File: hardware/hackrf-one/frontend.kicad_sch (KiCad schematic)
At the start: 141 parts, among them J2 RF-SHIELD-FRAME, J3 RF-SHIELD-COVER, J4 MOUNTING_HOLE, J5 MOUNTING_HOLE, J6 MOUNTING_HOLE, J7 MOUNTING_HOLE, J8 MOUNTING_HOLE, J9 MOUNTING_HOLE, P13 GPO1, P19 GPO3, P27 MIXER_SDATA, P31 MIXER_SCLK, P32 MIXER_ENX, P33 MIXER_RESETX, P34 MIX_BYPASS, P35 !MIX_BYPASS, P4 ANTENNA, P43 RX, P44 HP, P45 LP, P46 TX_MIX_BP, P47 RX_MIX_BP, P48 TX_AMP, P49 RX_AMP, P50 AMP_BYPASS, P51 !TX_AMP_PWR, P52 !RX_AMP_PWR, P6 GPO4, Q1 MOSFET_P, Q2 MOSFET_P, Q4 MOSFET_P, T1 MIX_IN_BALUN, T2 MIX_OUT_BALUN, U1 SKY13453, U10 SKY13453, U11 SKY13453, U12 SKY13317, U13 MGA-81563, U14 SKY13317, U2 SKY13453, U25 MGA-81563, U3 RX_LOWPASS_FILTER, U4 RFFC5072, U5 SKY13453, U6 SKY13453, U7 SKY13453, U8 RX_HIGHPASS_FILTER, U9 SKY13317

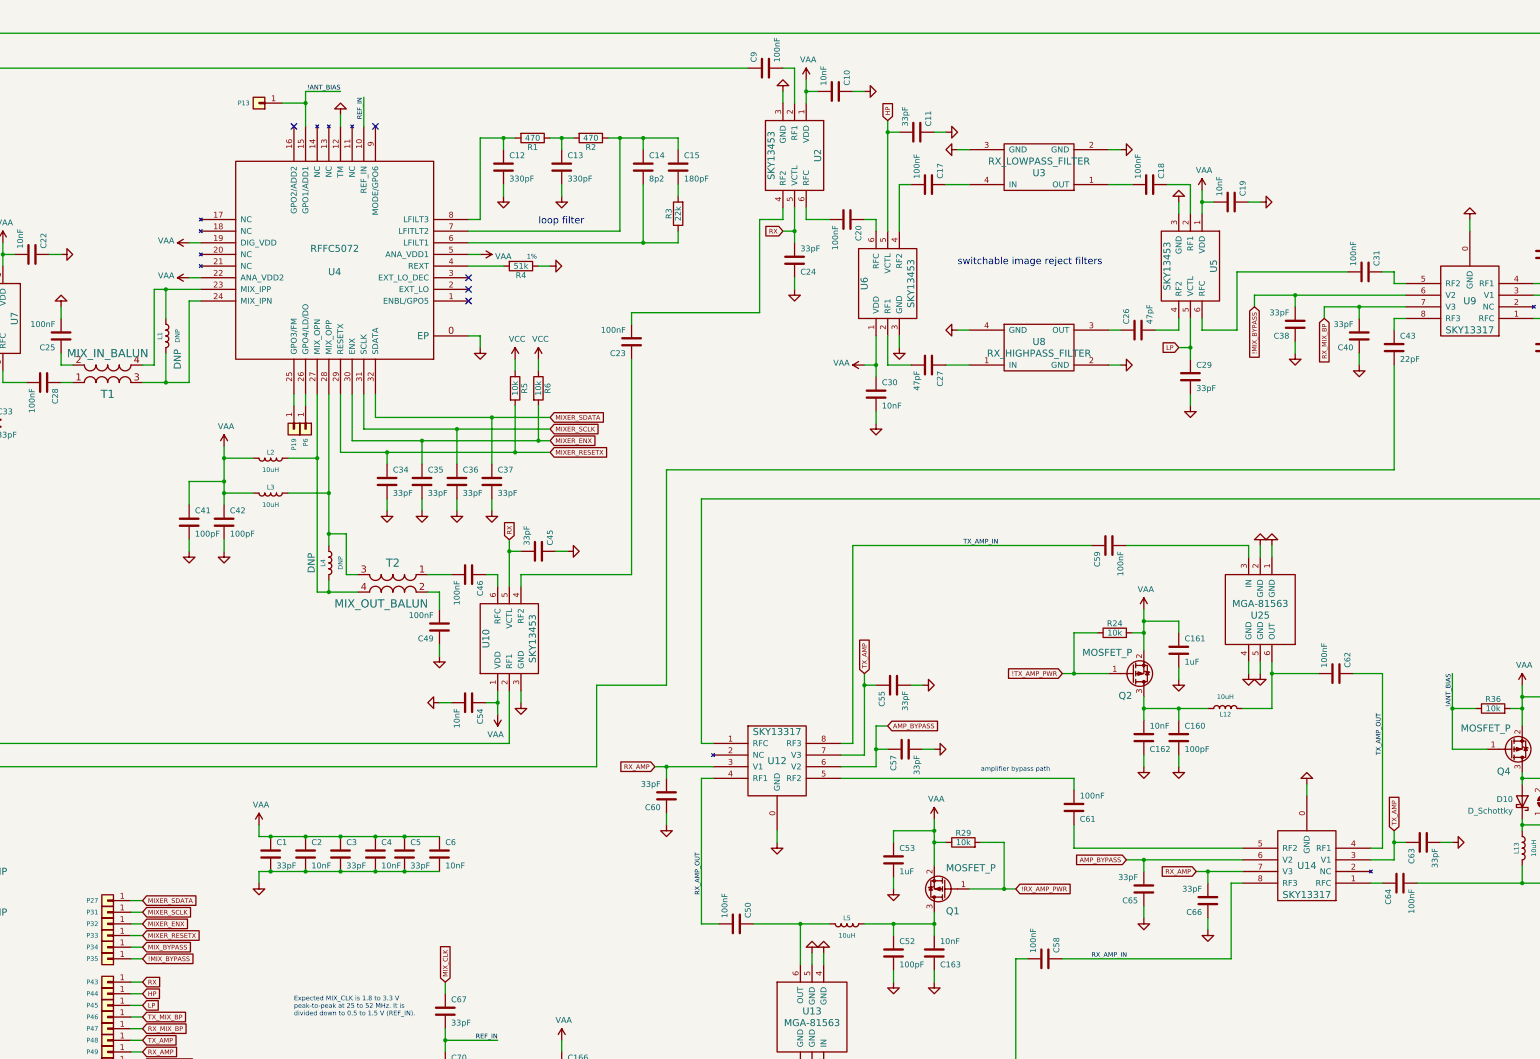
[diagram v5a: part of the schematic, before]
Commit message: HackRF One: move !ANT_BIAS control from U4 to U23
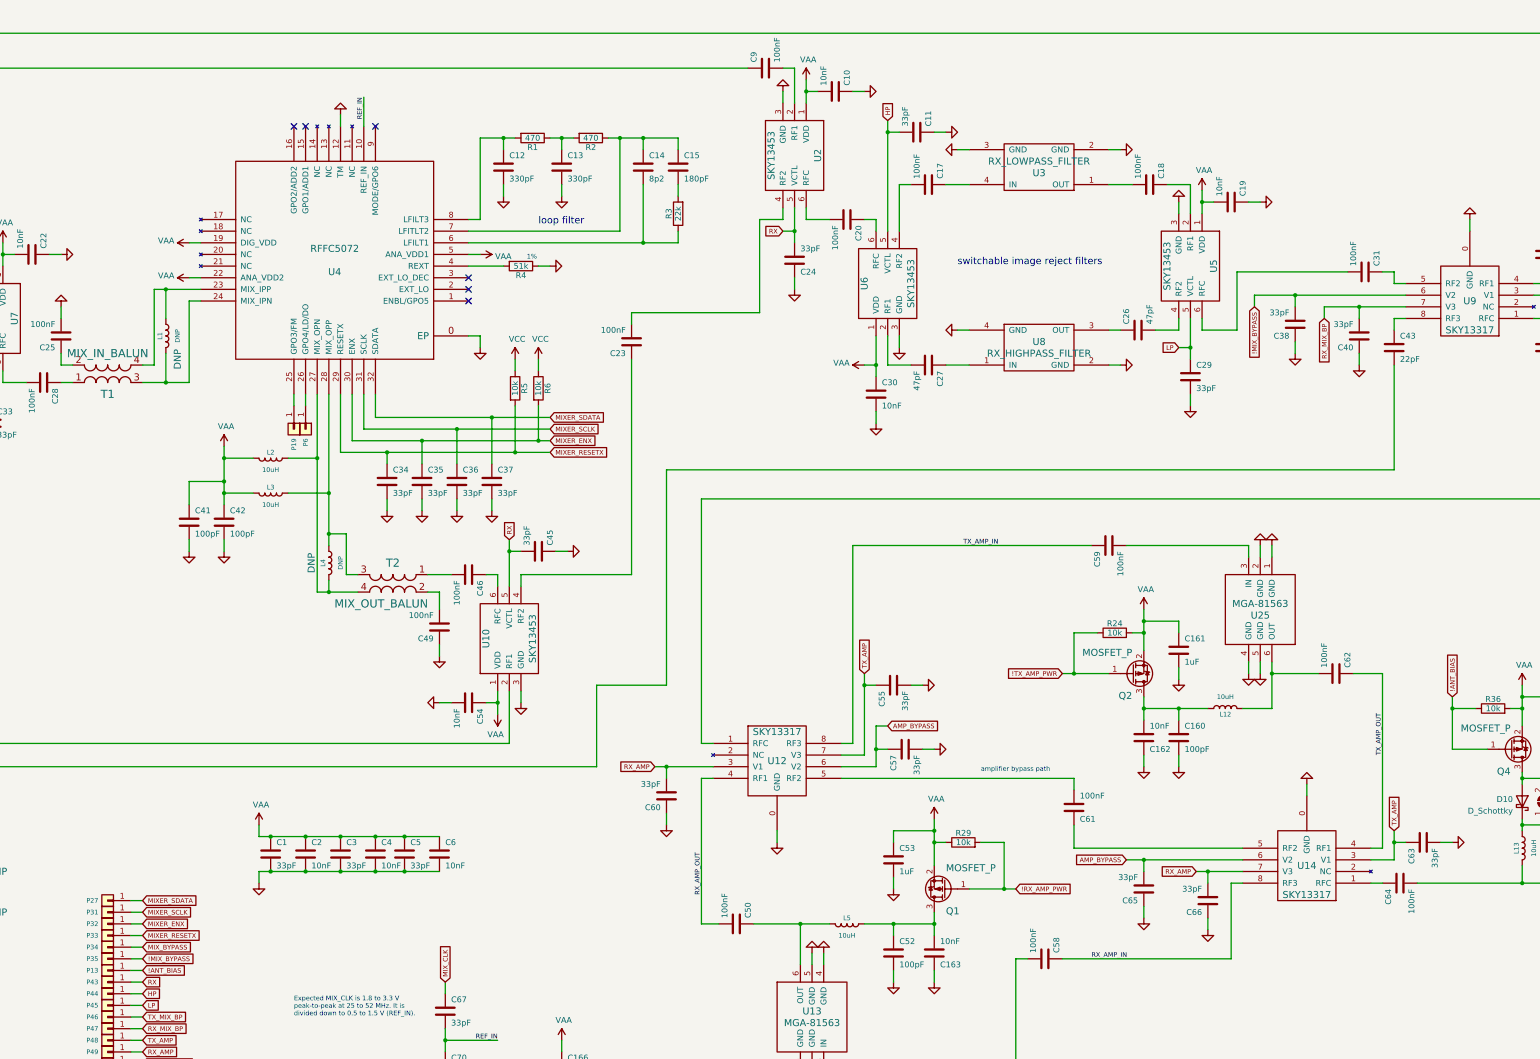
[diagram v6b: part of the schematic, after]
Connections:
- net !ANT_BIAS: no longer U4.15 (GPO1/ADD1)
- no-connect marks 5 -> 6
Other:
- moved on the sheet: P13
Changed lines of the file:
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@@
   (junction (at 160.02 248.92) (diameter 0) (color 0 0 0 0)
   )
-  (junction (at 129.54 44.45) (diameter 0) (color 0 0 0 0)
-  )
   (junction (at 111.76 129.54) (diameter 0) (color 0 0 0 0)
   )
@@
   (no_connect (at 165.1 85.09))
   (no_connect (at 165.1 87.63))
+  (no_connect (at 129.54 49.53))
   (no_connect (at 127 49.53))
   (no_connect (at 144.78 49.53))
@@
     (stroke (width 0) (type default) (color 0 0 0 0))
   )
-  (wire (pts (xy 124.46 44.45) (xy 129.54 44.45))
-    (stroke (width 0) (type default) (color 0 0 0 0))
-  )
   (wire (pts (xy 237.49 223.52) (xy 243.84 223.52))
     (stroke (width 0) (type default) (color 0 0 0 0))
@@
     (stroke (width 0) (type default) (color 0 0 0 0))
   )
-  (wire (pts (xy 129.54 44.45) (xy 129.54 49.53))
-    (stroke (width 0) (type default) (color 0 0 0 0))
-  )
   (wire (pts (xy 147.32 120.65) (xy 175.26 120.65))
     (stroke (width 0) (type default) (color 0 0 0 0))
@@
     (stroke (width 0) (type default) (color 0 0 0 0))
   )
+  (wire (pts (xy 91.44 233.68) (xy 93.98 233.68))
+    (stroke (width 0) (type default) (color 0 0 0 0))
+  )
   (wire (pts (xy 31.75 254) (xy 31.75 256.54))
     (stroke (width 0) (type default) (color 0 0 0 0))
@@
     (stroke (width 0) (type default) (color 0 0 0 0))
   )
-  (wire (pts (xy 129.54 41.91) (xy 137.16 41.91))
-    (stroke (width 0) (type default) (color 0 0 0 0))
-  )
   (wire (pts (xy 134.62 148.59) (xy 134.62 151.13))
     (stroke (width 0) (type default) (color 0 0 0 0))
@@
     (stroke (width 0) (type default) (color 0 0 0 0))
   )
-  (wire (pts (xy 379.73 168.91) (xy 379.73 176.53))
+  (wire (pts (xy 379.73 173.99) (xy 379.73 176.53))
     (stroke (width 0) (type default) (color 0 0 0 0))
   )
@@
     (stroke (width 0) (type default) (color 0 0 0 0))
   )
-  (wire (pts (xy 129.54 41.91) (xy 129.54 44.45))
-    (stroke (width 0) (type default) (color 0 0 0 0))
-  )
   (wire (pts (xy 271.78 93.98) (xy 274.32 93.98))
     (stroke (width 0) (type default) (color 0 0 0 0))
@@
     (effects (font (size 1.016 1.016)) (justify right bottom))
   )
-  (label "!ANT_BIAS" (at 379.73 168.91 270)
-    (effects (font (size 1.016 1.016)) (justify right bottom))
-  )
   (label "TX_AMP_IN" (at 280.67 140.97 180)
     (effects (font (size 1.016 1.016)) (justify right bottom))
   )
-  (label "!ANT_BIAS" (at 137.16 41.91 180)
-    (effects (font (size 1.016 1.016)) (justify right bottom))
-  )
   (label "REF_IN" (at 142.24 43.18 270)
     (effects (font (size 1.016 1.016)) (justify right bottom))
@@
     )
   )
+  (global_label "!ANT_BIAS" (shape input) (at 93.98 233.68 0) (fields_autoplaced)
+    (effects (font (size 1.016 1.016)) (justify left))
+    (property "Intersheet References" "${INTERSHEET_REFS}" (id 0) (at 103.1448 233.6165 0)
+      (effects (font (size 1.016 1.016)) (justify left) hide)
+    )
+  )
   (global_label "TX_IF" (shape input) (at 27.94 29.21 180) (fields_autoplaced)
     (effects (font (size 1.524 1.524)) (justify right))
@@
     )
   )
+  (global_label "!ANT_BIAS" (shape input) (at 379.73 173.99 90) (fields_autoplaced)
+    (effects (font (size 1.016 1.016)) (justify left))
+    (property "Intersheet References" "${INTERSHEET_REFS}" (id 0) (at 379.6665 164.8252 90)
+      (effects (font (size 1.016 1.016)) (justify left) hide)
+    )
+  )
   (global_label "!MIX_BYPASS" (shape input) (at 43.18 22.86 90) (fields_autoplaced)
     (effects (font (size 1.016 1.016)) (justify left))
@@
     (pin "1")
   )
-  (symbol (lib_id "Connector_Generic:Conn_01x01") (at 119.38 44.45 180) (unit 1)
+  (symbol (lib_id "Connector_Generic:Conn_01x01") (at 86.36 233.68 180) (unit 1)
     (in_bom yes) (on_board yes)
-    (property "Reference" "P13" (id 0) (at 117.348 44.45 0)
+    (property "Reference" "P13" (id 0) (at 84.328 233.68 0)
       (effects (font (size 1.016 1.016)) (justify left))
     )
-    (property "Value" "GPO1" (id 1) (at 119.38 45.847 0)
+    (property "Value" "GPO1" (id 1) (at 86.36 235.077 0)
       (effects (font (size 0.762 0.762)) hide)
     )
-    (property "Footprint" "hackrf:GSG-TESTPOINT-50MIL" (id 2) (at 119.38 44.45 0)
+    (property "Footprint" "hackrf:GSG-TESTPOINT-50MIL" (id 2) (at 86.36 233.68 0)
       (effects (font (size 1.524 1.524)) hide)
     )
-    (property "Datasheet" "" (id 3) (at 119.38 44.45 0)
+    (property "Datasheet" "" (id 3) (at 86.36 233.68 0)
       (effects (font (size 1.524 1.524)) hide)
     )
-    (property "Note" "DNP" (id 4) (at 119.38 44.45 0)
+    (property "Note" "DNP" (id 4) (at 86.36 233.68 0)
       (effects (font (size 1.524 1.524)) hide)
     )

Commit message: HackRF One: component selections, DNP, and Notes
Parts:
- C1, C11, C24, C29, C3, C33, C34, C35, C36, C37, C38, C39, C40, C45, C47, C5, C55, C57, C60, C63, C65, C66, C67, C7: Manufacturer Murata -> Samsung; Part Number GRM1555C1H330JA01D -> CL05C330JB5NNNC
- C10, C16, C162, C163, C19, C2, C22, C30, C4, C54, C56, C6: Manufacturer Murata -> Samsung; Part Number GRM155R71C103KA01D -> CL05B103KB5NNNC
- C12, C13: Manufacturer Murata -> Samsung; Part Number GRM155R71H331KA01D -> CL05C331JB5NNNC
- C14: Manufacturer Taiyo Yuden -> Yageo; Part Number UMK105CG8R2DV-F -> CC0402CRNPO9BN8R2
- C15: Manufacturer Murata -> Yageo; Part Number GRM1555C1H181JA01D -> CC0402JRNPO9BN181
- C160, C41, C42, C52, C70: Manufacturer Murata -> Samsung; Part Number GRM1555C1H101JA01D -> CL05C101JB5NNNC
- C161, C171, C53: Manufacturer Taiyo Yuden -> Samsung; Part Number LMK105BJ105KV-F -> CL05A105KP5NNNC
- C21, C32, C43, C48, C51, C8: Manufacturer Murata -> Samsung; Part Number GRM1555C1H220JA01D -> CL05C220JB5NNNC
- C26, C27: Manufacturer Murata -> Samsung; Part Number GRM1555C1H470JA01D -> CL05C470JB5NNNC
- J2, J3, J4, J5, J6, J7, J8, J9, L1, L4, P13, P19, P27, P31, P32, P33, P34, P35, P43, P44, P45, P46, P47, P48, P49, P50, P51, P52, P6: DNP (none) -> DNP; Note DNP -> (none)
- JP1: DNP (none) -> DNP
- Q1, Q2, Q4: Manufacturer Fairchild -> Yangzhou Yangjie; Part Number BSS84 -> YJL2301C

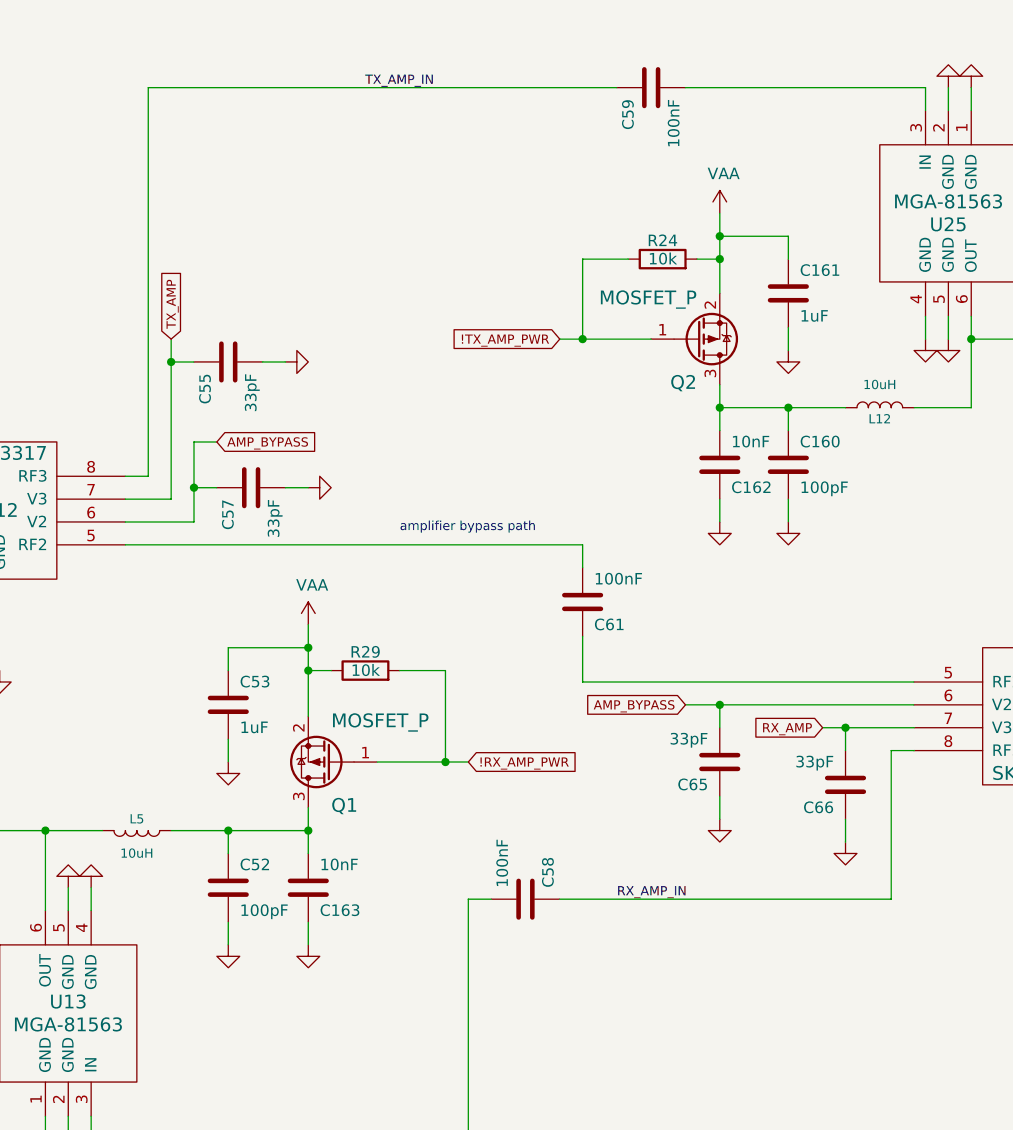
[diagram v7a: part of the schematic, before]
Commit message: HackRF One: add resistance to amplifier supplies
This may improve reliability since switching to a MOSFET with lower on
resistance.
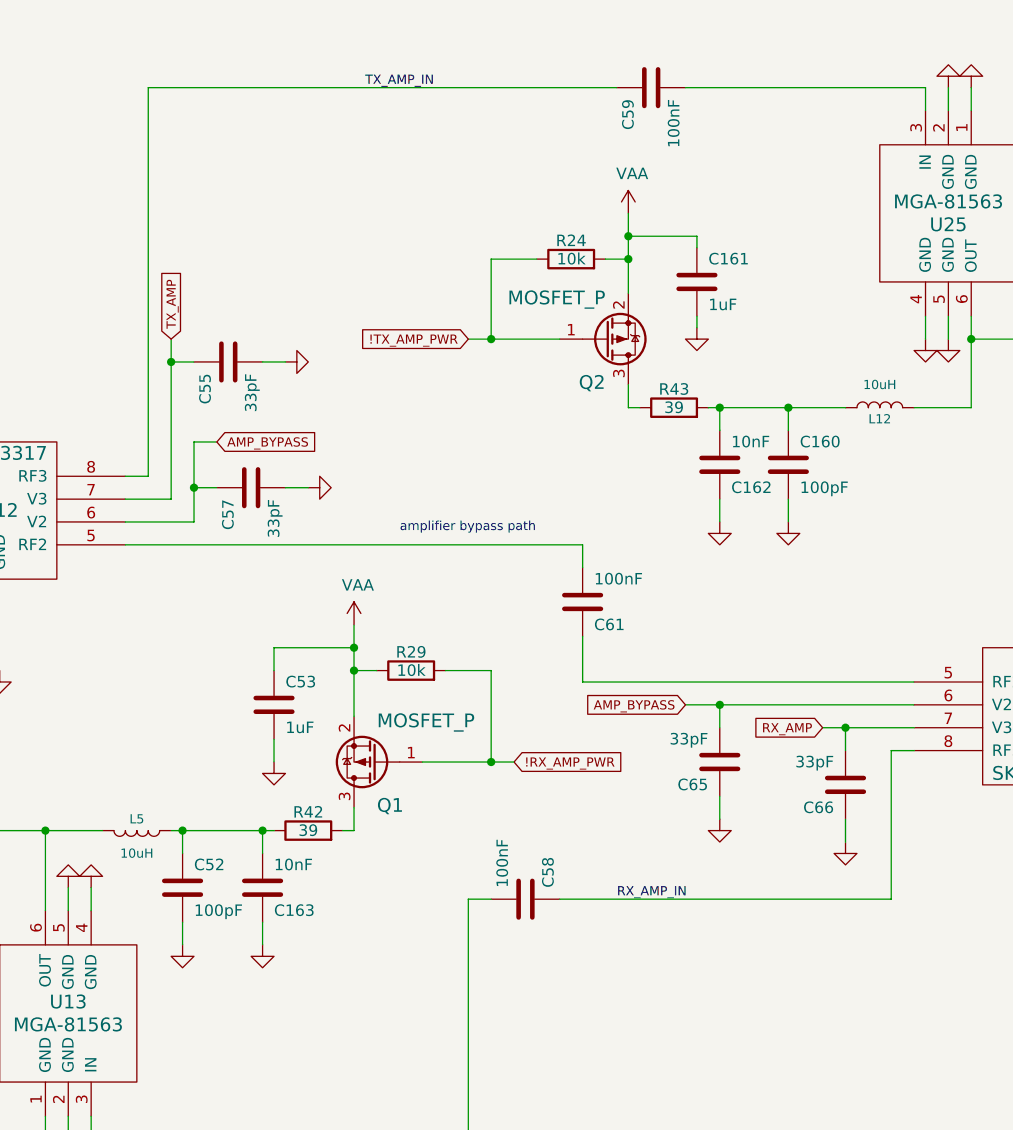
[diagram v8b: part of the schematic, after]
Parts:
- added R42, R43: 39, hackrf:GSG-0402, symbol Device:R
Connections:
- net at C163.2, C52.1, L5.1: now also R42.1; no longer Q1.3 (D)
- net at C160.1, C162.2, L12.1: now also R43.2; no longer Q2.3 (D)
- new net: Q1.3 (D), R42.2
- new net: Q2.3 (D), R43.1
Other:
- moved on the sheet: C161, C163, C52, C53, Q1, Q2, R24, R29
